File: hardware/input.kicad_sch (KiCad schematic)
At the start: 5 parts, among them U3 INA228

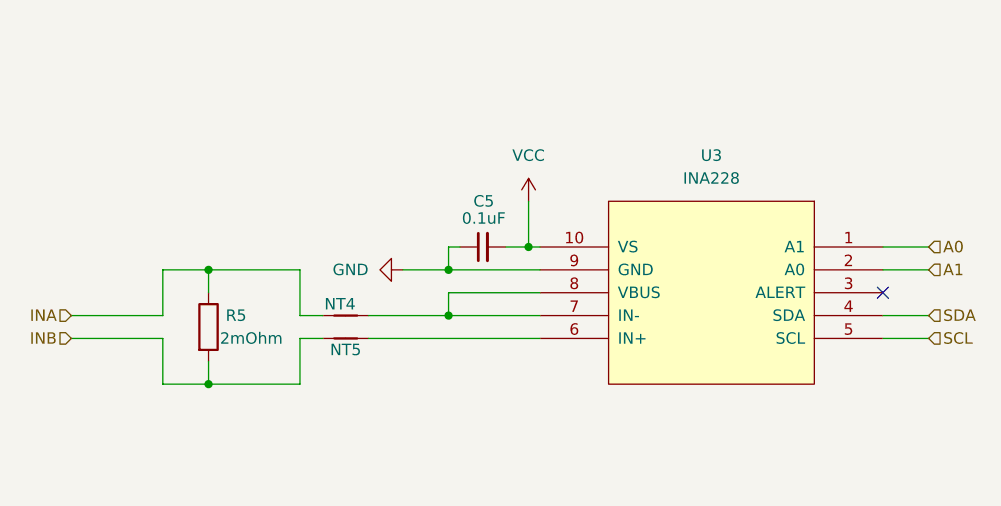
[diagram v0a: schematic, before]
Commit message: Remove PLC, use ESP
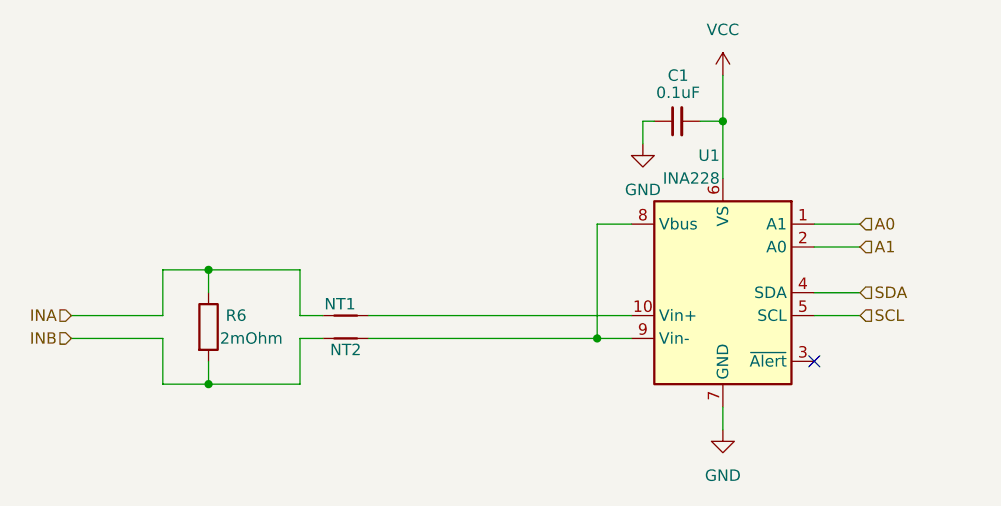
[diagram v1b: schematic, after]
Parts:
- NT1: renamed from NT4; footprint hardware:NetTie-2_SMD_Pad0.25mm -> footprints:NetTie-2_SMD_Pad0.25mm
- NT2: renamed from NT5; footprint hardware:NetTie-2_SMD_Pad0.25mm -> footprints:NetTie-2_SMD_Pad0.25mm
- U1: renamed from U3; symbol INA228:INA228 -> symbols:INA228
- renumbered C5 to C1, R5 to R6
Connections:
- net GND: now also U1.7 (GND); no longer U1.9 (GND)
- net VCC: now also U1.6 (VS); no longer U1.10 (VS)
- net at NT2.2: now also U1.8 (Vbus), U1.9 (Vin-); no longer U1.6 (IN+)
- new net: NT1.2, U1.10 (Vin+)
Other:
- moved on the sheet: C1, U1
